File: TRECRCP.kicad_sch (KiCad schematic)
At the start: 16 parts, among them J1 Raspberry_Pi_4, SW1 Dispatch2, SW4 Restart, SW5 Dispatch1, SW6 3 position key switch, SW7 Maintanance rotary switch, SW8 Stop

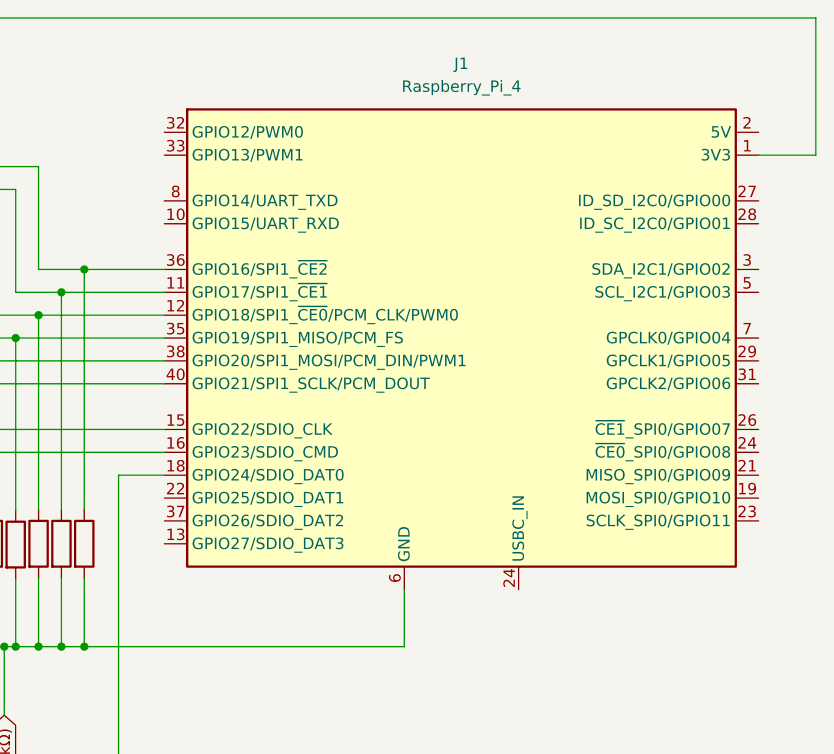
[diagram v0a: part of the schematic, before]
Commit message: Deleted Raspberry pi
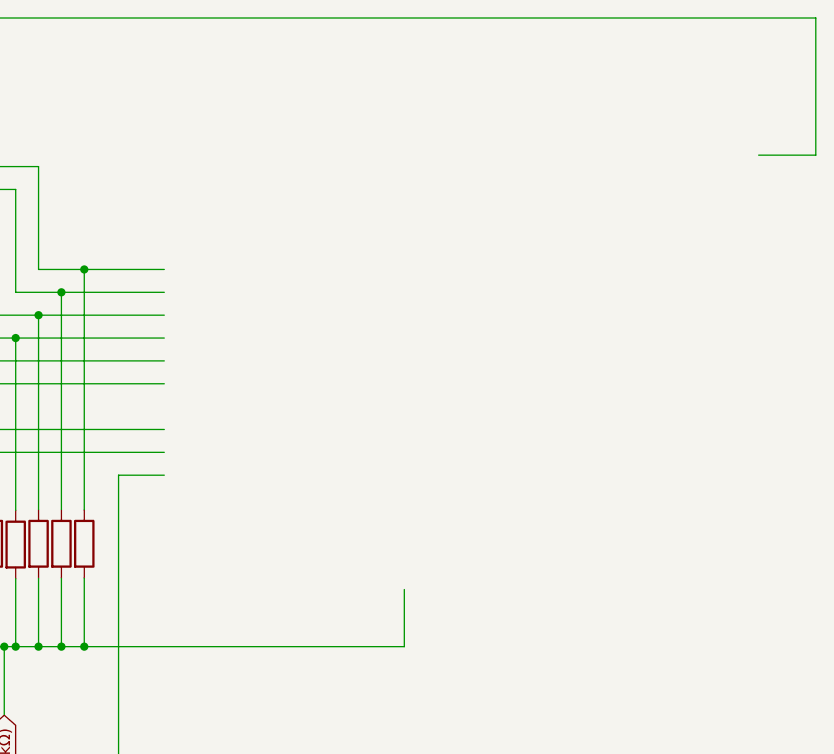
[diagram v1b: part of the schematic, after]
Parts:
- removed J1: Raspberry_Pi_4, symbol Connector:Raspberry_Pi_4
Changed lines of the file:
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@@
-	)
-	(symbol
-		(lib_id "Connector:Raspberry_Pi_4")
-		(at 142.24 73.66 0)
-		(unit 1)
-		(exclude_from_sim no)
-		(in_bom yes)
-		(on_board yes)
-		(dnp no)
-		(fields_autoplaced yes)
-		(property "Reference" "J1"
-			(at 142.24 43.18 0)
-			(effects
-				(font
-					(size 1.27 1.27)
-				)
-			)
-		)
-		(property "Value" "Raspberry_Pi_4"
-			(at 142.24 45.72 0)
-			(effects
-				(font
-					(size 1.27 1.27)
-				)
-			)
-		)
-		(property "Footprint" ""
-			(at 212.344 121.158 0)
-			(effects
-				(font
-					(size 1.27 1.27)
-				)
-				(justify left)
-				(hide yes)
-			)
-		)
-		(property "Datasheet" "https://datasheets.raspberrypi.com/rpi4/raspberry-pi-4-datasheet.pdf"
-			(at 157.988 105.918 0)
-			(effects
-				(font
-					(size 1.27 1.27)
-				)
-				(justify left)
-				(hide yes)
-			)
-		)
-		(property "Description" "Raspberry Pi 4 Model B"
-			(at 157.988 103.378 0)
-			(effects
-				(font
-					(size 1.27 1.27)
-				)
-				(justify left)
-				(hide yes)
-			)
-		)
-		(pin "35"
-		)
-		(pin "15"
-		)
-		(pin "14"
-		)
-		(pin "8"
-		)
-		(pin "10"
-		)
-		(pin "32"
-		)
-		(pin "11"
-		)
-		(pin "33"
-		)
-		(pin "16"
-		)
-		(pin "38"
-		)
-		(pin "22"
-		)
-		(pin "37"
-		)
-		(pin "36"
-		)
-		(pin "13"
-		)
-		(pin "25"
-		)
-		(pin "12"
-		)
-		(pin "20"
-		)
-		(pin "40"
-		)
-		(pin "18"
-		)
-		(pin "30"
-		)
-		(pin "34"
-		)
-		(pin "39"
-		)
-		(pin "9"
-		)
-		(pin "2"
-		)
-		(pin "4"
-		)
-		(pin "1"
-		)
-		(pin "6"
-		)
-		(pin "17"
-		)
-		(pin "27"
-		)
-		(pin "19"
-		)
-		(pin "5"
-		)
-		(pin "31"
-		)
-		(pin "3"
-		)
-		(pin "29"
-		)
-		(pin "28"
-		)
-		(pin "24"
-		)
-		(pin "23"
-		)
-		(pin "21"
-		)
-		(pin "26"
-		)
-		(pin "7"
-		)
-		(pin "24"
-		)
-		(instances
-			(project ""
-				(path "/ea91bab5-2f80-490a-b9b5-c78a73310229"
-					(reference "J1")
-					(unit 1)
-				)
-			)
-		)
 	)
 	(symbol

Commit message: Revert "Deleted Raspberry pi"
This reverts commit ef78a613efe69fcbedc783515965194093190659.
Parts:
- added J1: Raspberry_Pi_4, symbol Connector:Raspberry_Pi_4
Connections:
- net Drop Down Resistors(10kΩ): now also J1.6 (GND)
- net at R7.1, SW6.2: now also J1.11 (GPIO17/SPI1_~{CE1})
- net at R6.1, SW6.4: now also J1.12 (GPIO18/SPI1_~{CE0}/PCM_CLK/PWM0)
- net at R3.1, SW8.1: now also J1.40 (GPIO21/SPI1_SCLK/PCM_DOUT)
- net at ESTOP.1 (A), SW4.2, SW5.2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: now also J1.1 (3V3), J1.17 (3V3)
- net at R8.1, SW6.1: now also J1.36 (GPIO16/SPI1_~{CE2})
- net at ESTOP.2 (B): now also J1.18 (GPIO24/SDIO_DAT0)
- net at R5.1, SW1.1: now also J1.35 (GPIO19/SPI1_MISO/PCM_FS)
- net at R4.1, SW4.1: now also J1.38 (GPIO20/SPI1_MOSI/PCM_DIN/PWM1)
- net at R2.1, SW7.1: now also J1.15 (GPIO22/SDIO_CLK)
- net at R1.1, SW7.4: now also J1.16 (GPIO23/SDIO_CMD)
- new net: J1.14 (GND), J1.20 (GND), J1.25 (GND), J1.30 (GND), J1.34 (GND), J1.39 (GND), J1.9 (GND)
- new net: J1.2 (5V), J1.4 (5V)
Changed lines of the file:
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@@
+	)
+	(symbol
+		(lib_id "Connector:Raspberry_Pi_4")
+		(at 142.24 73.66 0)
+		(unit 1)
+		(exclude_from_sim no)
+		(in_bom yes)
+		(on_board yes)
+		(dnp no)
+		(fields_autoplaced yes)
+		(property "Reference" "J1"
+			(at 142.24 43.18 0)
+			(effects
+				(font
+					(size 1.27 1.27)
+				)
+			)
+		)
+		(property "Value" "Raspberry_Pi_4"
+			(at 142.24 45.72 0)
+			(effects
+				(font
+					(size 1.27 1.27)
+				)
+			)
+		)
+		(property "Footprint" ""
+			(at 212.344 121.158 0)
+			(effects
+				(font
+					(size 1.27 1.27)
+				)
+				(justify left)
+				(hide yes)
+			)
+		)
+		(property "Datasheet" "https://datasheets.raspberrypi.com/rpi4/raspberry-pi-4-datasheet.pdf"
+			(at 157.988 105.918 0)
+			(effects
+				(font
+					(size 1.27 1.27)
+				)
+				(justify left)
+				(hide yes)
+			)
+		)
+		(property "Description" "Raspberry Pi 4 Model B"
+			(at 157.988 103.378 0)
+			(effects
+				(font
+					(size 1.27 1.27)
+				)
+				(justify left)
+				(hide yes)
+			)
+		)
+		(pin "35"
+		)
+		(pin "15"
+		)
+		(pin "14"
+		)
+		(pin "8"
+		)
+		(pin "10"
+		)
+		(pin "32"
+		)
+		(pin "11"
+		)
+		(pin "33"
+		)
+		(pin "16"
+		)
+		(pin "38"
+		)
+		(pin "22"
+		)
+		(pin "37"
+		)
+		(pin "36"
+		)
+		(pin "13"
+		)
+		(pin "25"
+		)
+		(pin "12"
+		)
+		(pin "20"
+		)
+		(pin "40"
+		)
+		(pin "18"
+		)
+		(pin "30"
+		)
+		(pin "34"
+		)
+		(pin "39"
+		)
+		(pin "9"
+		)
+		(pin "2"
+		)
+		(pin "4"
+		)
+		(pin "1"
+		)
+		(pin "6"
+		)
+		(pin "17"
+		)
+		(pin "27"
+		)
+		(pin "19"
+		)
+		(pin "5"
+		)
+		(pin "31"
+		)
+		(pin "3"
+		)
+		(pin "29"
+		)
+		(pin "28"
+		)
+		(pin "24"
+		)
+		(pin "23"
+		)
+		(pin "21"
+		)
+		(pin "26"
+		)
+		(pin "7"
+		)
+		(pin "24"
+		)
+		(instances
+			(project ""
+				(path "/ea91bab5-2f80-490a-b9b5-c78a73310229"
+					(reference "J1")
+					(unit 1)
+				)
+			)
+		)
 	)
 	(symbol

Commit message: add raspi
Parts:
- removed J1: Raspberry_Pi_4, symbol Connector:Raspberry_Pi_4
- added RCC1: ~, symbol TREC SYMBOL LIB:Raspbery_Pi_5
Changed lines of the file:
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@@
-	)
-	(junction
-		(at 100.33 107.95)
-		(diameter 0)
-		(color 255 244 63 1)
 	)
 	(junction
@@
 	(wire
 		(pts
-			(xy 100.33 107.95) (xy 135.89 107.95)
-		)
-		(stroke
-			(width 0)
-			(type default)
-			(color 255 244 63 1)
-		)
-	)
-	(wire
-		(pts
 			(xy 92.71 100.4179) (xy 92.71 107.95)
 		)
@@
 			(type default)
 			(color 255 244 63 1)
-		)
-	)
-	(wire
-		(pts
-			(xy 135.89 101.6) (xy 135.89 107.95)
-		)
-		(stroke
-			(width 0)
-			(type default)
-			(color 255 255 0 1)
 		)
 	)
@@
 	)
 	(symbol
-		(lib_id "Connector:Raspberry_Pi_4")
-		(at 142.24 73.66 0)
+		(lib_id "TREC SYMBOL LIB:Raspbery_Pi_5")
+		(at 149.86 92.71 0)
 		(unit 1)
 		(exclude_from_sim no)
@@
 		(dnp no)
 		(fields_autoplaced yes)
-		(property "Reference" "J1"
-			(at 142.24 43.18 0)
-			(effects
-				(font
-					(size 1.27 1.27)
-				)
-			)
-		)
-		(property "Value" "Raspberry_Pi_4"
-			(at 142.24 45.72 0)
+		(property "Reference" "RCC1"
+			(at 152.4 59.69 0)
+			(effects
+				(font
+					(size 1.27 1.27)
+				)
+			)
+		)
+		(property "Value" "~"
+			(at 152.4 62.23 0)
 			(effects
 				(font
@@
 		)
 		(property "Footprint" ""
-			(at 212.344 121.158 0)
-			(effects
-				(font
-					(size 1.27 1.27)
-				)
-				(justify left)
-				(hide yes)
-			)
-		)
-		(property "Datasheet" "https://datasheets.raspberrypi.com/rpi4/raspberry-pi-4-datasheet.pdf"
-			(at 157.988 105.918 0)
-			(effects
-				(font
-					(size 1.27 1.27)
-				)
-				(justify left)
-				(hide yes)
-			)
-		)
-		(property "Description" "Raspberry Pi 4 Model B"
-			(at 157.988 103.378 0)
-			(effects
-				(font
-					(size 1.27 1.27)
-				)
-				(justify left)
-				(hide yes)
-			)
+			(at 149.86 92.71 0)
+			(effects
+				(font
+					(size 1.27 1.27)
+				)
+				(hide yes)
+			)
+		)
+		(property "Datasheet" ""
+			(at 149.86 92.71 0)
+			(effects
+				(font
+					(size 1.27 1.27)
+				)
+				(hide yes)
+			)
+		)
+		(property "Description" ""
+			(at 149.86 92.71 0)
+			(effects
+				(font
+					(size 1.27 1.27)
+				)
+				(hide yes)
+			)
+		)
+		(pin "26"
+		)
+		(pin "24"
+		)
+		(pin "40"
+		)
+		(pin "38"
+		)
+		(pin "30"
+		)
+		(pin "28"
+		)
+		(pin "36"
+		)
+		(pin "34"
+		)
+		(pin "32"
+		)
+		(pin "2"
+		)
+		(pin "4"
+		)
+		(pin "10"
+		)
+		(pin "8"
+		)
+		(pin "6"
+		)
+		(pin "18"
+		)
+		(pin "22"
+		)
+		(pin "20"
+		)
+		(pin "1"
+		)
+		(pin "17"
+		)
+		(pin "5"
+		)
+		(pin "3"
+		)
+		(pin "7"
+		)
+		(pin "9"
+		)
+		(pin "19"
+		)
+		(pin "13"
+		)
+		(pin "15"
+		)
+		(pin "11"
+		)
+		(pin "27"
+		)
+		(pin "21"
+		)
+		(pin "31"
+		)
+		(pin "29"
+		)
+		(pin "23"
+		)
+		(pin "25"
+		)
+		(pin "14"
+		)
+		(pin "16"
+		)
+		(pin "12"
+		)
+		(pin "33"
 		)
 		(pin "35"
 		)
-		(pin "15"
-		)
-		(pin "14"
-		)
-		(pin "8"
-		)
-		(pin "10"
-		)
-		(pin "32"
-		)
-		(pin "11"
-		)
-		(pin "33"
-		)
-		(pin "16"
-		)
-		(pin "38"
-		)
-		(pin "22"
+		(pin "39"
 		)
 		(pin "37"
-		)
-		(pin "36"
-		)
-		(pin "13"
-		)
-		(pin "25"
-		)
-		(pin "12"
-		)
-		(pin "20"
-		)
-		(pin "40"
-		)
-		(pin "18"
-		)
-		(pin "30"
-		)
-		(pin "34"
-		)
-		(pin "39"
-		)
-		(pin "9"
-		)
-		(pin "2"
-		)
-		(pin "4"
-		)
-		(pin "1"
-		)
-		(pin "6"
-		)
-		(pin "17"
-		)
-		(pin "27"
-		)
-		(pin "19"
-		)
-		(pin "5"
-		)
-		(pin "31"
-		)
-		(pin "3"
-		)
-		(pin "29"
-		)
-		(pin "28"
-		)
-		(pin "24"
-		)
-		(pin "23"
-		)
-		(pin "21"
-		)
-		(pin "26"
-		)
-		(pin "7"
-		)
-		(pin "24"
 		)
 		(instances
 			(project ""
 				(path "/ea91bab5-2f80-490a-b9b5-c78a73310229"
-					(reference "J1")
+					(reference "RCC1")
 					(unit 1)
 				)

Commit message: Cleanup RCC
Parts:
- removed SW6: 3 position key switch, symbol Switch:SW_DP3T
- removed SW7: Maintanance rotary switch, symbol Switch:SW_DP3T
- added SW1: Key On/Off Switch, symbol Switch:SW_Rotary_1x3_MP
- added SW2: Maintenince Rotary Switch, symbol Switch:SW_Rotary_1x3_MP
- R8: value R -> 100k
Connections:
- net Drop Down Resistors(10kΩ): now also R8.1, RCC1.39 (GND); no longer R8.2
- net Ride On: now reaches R7.1
- net Ride On: now also RCC1.7 (GPIO_4), SW1.1
- net Ride Maintenence: now reaches R6.1
- net Ride Maintenence: now also RCC1.11 (GPIO_17), SW1.3
- net at SW8.1: now also R1.1, RCC1.23 (GPIO_11); no longer R3.1
- net at ESTOP.1 (A), SW4.2, SW5.2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: now also RCC1.1 (3.3V), SW1.4, SW2.4
- net at ESTOP.2 (B): now also R8.2, RCC1.37 (GPIO_26)
- net at SW1.1: now also R3.1, RCC1.19 (GPIO_10); no longer R5.1
- net at SW4.1: now also R2.1, RCC1.21 (GPIO_9); no longer R4.1
- net Jog FWD: now reaches RCC1.13 (GPIO_27)
- net Jog FWD: now also R5.1, SW2.1
- net at RCC1.15 (GPIO_22): now also R4.1, SW2.3
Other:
- note added: "Dispatch"
- note added: "Jog BWD"
- note added: "Jog FWD"
- note added: "Restart"
- note added: "Ride Maintenence"
- note added: "Ride On"
- note added: "Ride Stop"
- moved on the sheet: ESTOP, RCC1
